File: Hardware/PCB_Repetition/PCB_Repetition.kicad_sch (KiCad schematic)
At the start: 45 parts, among them J1 Conn_01x03, SW1 SW_SPST, SW2 SW_SPST, U3 PCF8575DBR

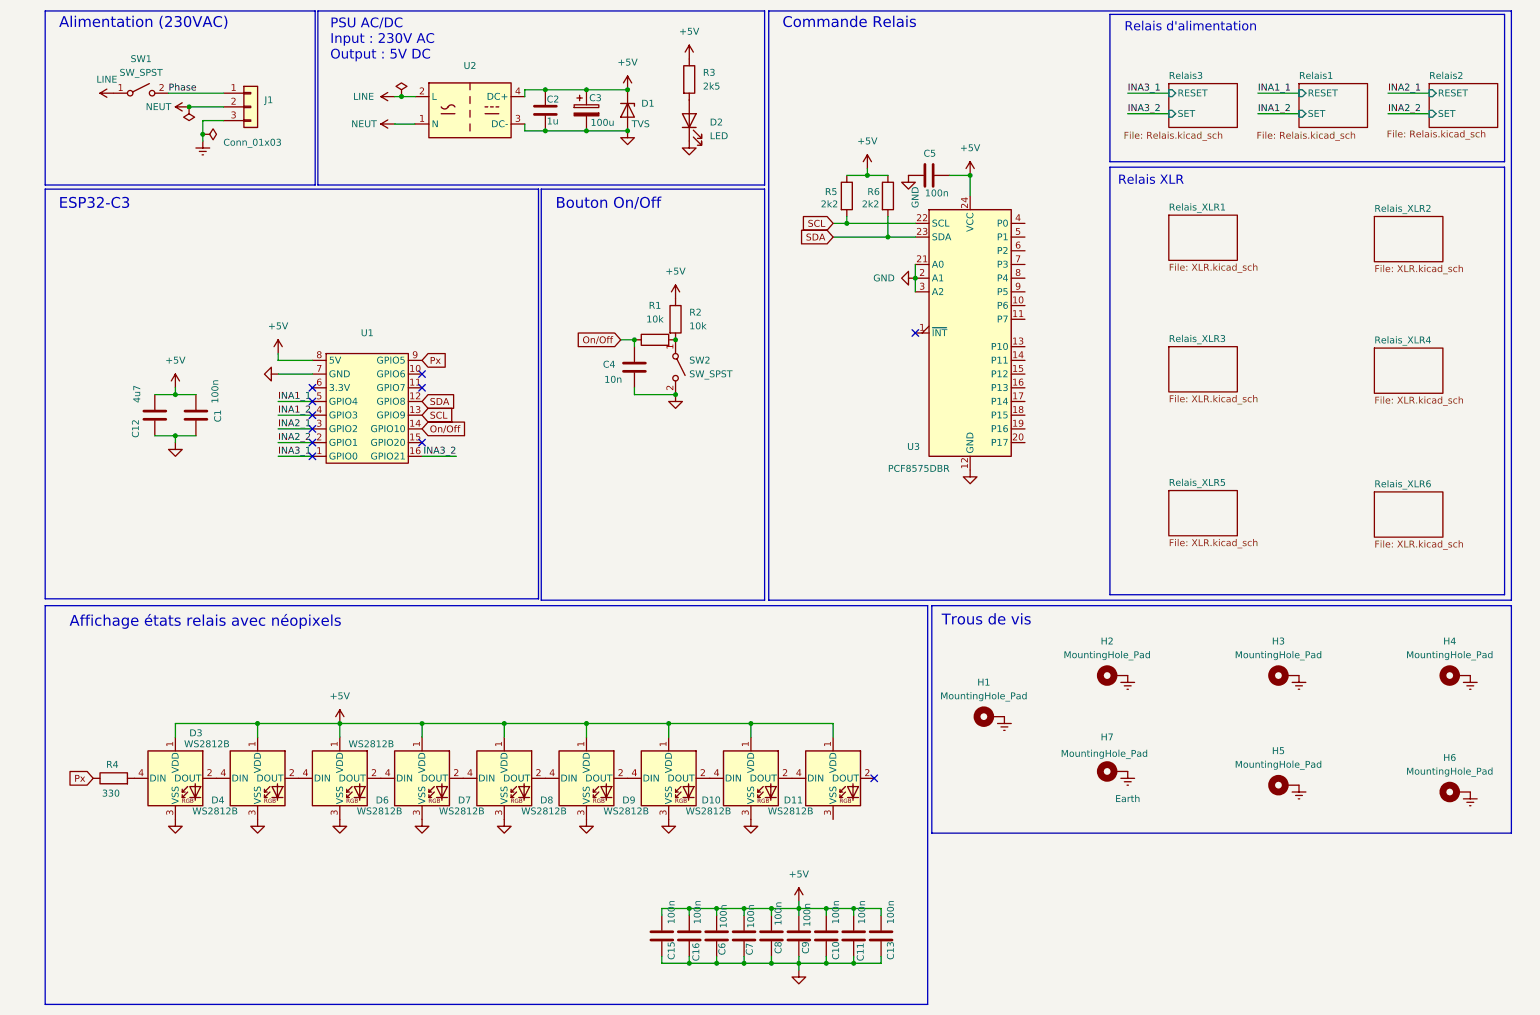
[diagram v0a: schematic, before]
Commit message: ajout des pulldown sur les transistors
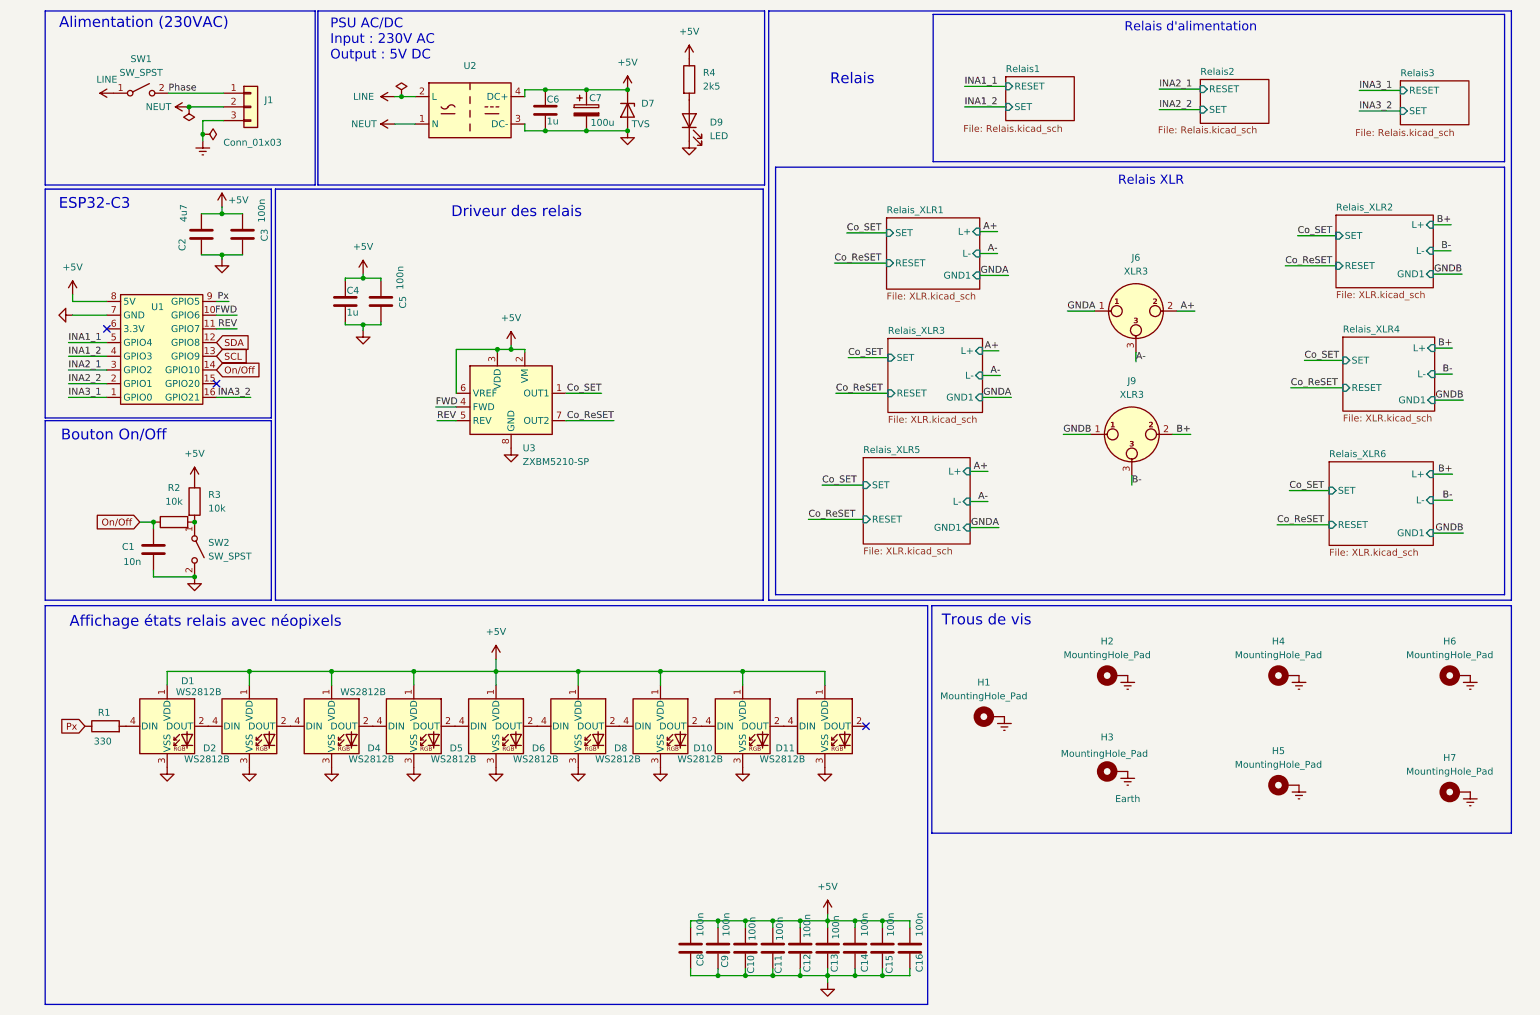
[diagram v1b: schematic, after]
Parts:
- removed R5, R6: 2k2, Resistor_SMD:R_0603_1608Metric_Pad0.98x0.95mm_HandSolder, symbol Device:R
- removed U3: PCF8575DBR, Package_SO:SSOP-24_5.3x8.2mm_P0.65mm, symbol Interface_Expansion:PCF8575DBR
- added C4: 1u, Capacitor_SMD:C_0201_0603Metric_Pad0.64x0.40mm_HandSolder, symbol Device:C
- added J6, J9: XLR3, Connector_Audio:Jack_XLR_Neutrik_NC3FAAV_Vertical, symbol Connector_Audio:XLR3
- added U3: ZXBM5210-SP, Package_SO:Diodes_SO-8EP, symbol Driver_Motor:ZXBM5210-SP
- renumbered C4 to C1, C6 to C10, C7 to C11, C8 to C12, C9 to C13, C10 to C14, C11 to C15, C13 to C16, C12 to C2, C1 to C3, C2 to C6, C3 to C7, C15 to C8, C16 to C9, D3 to D1, D4 to D2, D5 to D3, D6 to D4, D7 to D5, D8 to D6, D1 to D7, D9 to D8, D2 to D9, H7 to H3, H3 to H4, H4 to H6, H6 to H7, R4 to R1, R1 to R2, R2 to R3, R3 to R4
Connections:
- net +5V: now also C5.1, C4.1, U3.2 (VM), U3.3 (VDD), U3.6 (VREF); no longer C5.2
- net GND: now also C5.2, D11.3 (VSS), C4.2, U3.8 (GND), U3.9 (GND); no longer C5.1
- net FWD: now reaches U1.10 (GPIO6)
- net FWD: now also U3.4 (FWD)
- net REV: now reaches U1.11 (GPIO7)
- net REV: now also U3.5 (REV)
- new net A+: J6.2
- new net A-: J6.3
- new net B+: J9.2
- new net B-: J9.3
- new net Co_ReSET: U3.7 (OUT2)
- new net Co_SET: U3.1 (OUT1)
- new net GNDA: J6.1
- new net GNDB: J9.1
- no-connect marks 11 -> 3
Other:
- sheet Relais_XLR1 ports: added GND1, L+, L-, RESET, SET; removed none
- sheet Relais_XLR2 ports: added GND1, L+, L-, RESET, SET; removed none
- sheet Relais_XLR3 ports: added GND1, L+, L-, RESET, SET; removed none
- sheet Relais_XLR4 ports: added GND1, L+, L-, RESET, SET; removed none
- sheet Relais_XLR5 ports: added GND1, L+, L-, RESET, SET; removed none
- sheet Relais_XLR6 ports: added GND1, L+, L-, RESET, SET; removed none
- note added: "Driveur des relais"
- note added: "Relais"
- note removed: "Commande Relais"
- moved on the sheet: C1, C10, C11, C12, C13, C14, C15, C16, C2, C3, C8, C9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

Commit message: finalisation PCB-salle de Répétition
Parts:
- removed U1: ~, ESP32_C3_SuperMini:SuperMini SMT, symbol ESP32_C3_SuperMini:SuperMini_1
- removed U2: ~, AC_DC_module:MP-LDE06-20B05, symbol AC-DC-5V:U_1
- added C17, C18: 100n, Capacitor_SMD:C_0603_1608Metric_Pad1.08x0.95mm_HandSolder, symbol Device:C
- added D12: WS2812B, LED_SMD:LED_WS2812B_PLCC4_5.0x5.0mm_P3.2mm, symbol LED:WS2812B
- added R5, R6: 2k2, Resistor_SMD:R_0603_1608Metric_Pad0.98x0.95mm_HandSolder, symbol Device:R
- added U1: ~, ESP32_SuperMini:SuperMini SMT, symbol ESP32_C3:SuperMini_1
- added U3: ~, AD-DC_Module:MP-LDE06-20B05, symbol Module_AC_DC:U_1
- added U4: PCF8575DBR, Package_SO:SSOP-24_5.3x8.2mm_P0.65mm, symbol Interface_Expansion:PCF8575DBR
- C4, C6: footprint Capacitor_SMD:C_0201_0603Metric_Pad0.64x0.40mm_HandSolder -> Capacitor_SMD:C_0603_1608Metric_Pad1.08x0.95mm_HandSolder
- J1: footprint Conn_Alim:Conn_Secteur -> Conn_secteur:Conn_Secteur
- renumbered J9 to J2, J6 to J3, U3 to U2
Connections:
- net +5V: now also C17.2, C18.1, D12.1 (VDD), R5.1, R6.1, U1.8 (5V), U3.4 (DC+), U4.24 (VCC)
- net Earth: no longer H1.1, H2.1, H4.1, H5.1, H6.1, H7.1
- net FWD: now also U1.10 (GPIO6)
- net GND: now also H1.1, H4.1, H5.1, H6.1, H7.1, C17.1, C18.2, D12.3 (VSS), U1.7 (GND), U3.3 (DC-), U4.12 (GND), U4.2 (A1), U4.21 (A0), U4.3 (A2)
- net INA1_1: now also U4.9 (P5)
- net INA1_2: now also U4.8 (P4)
- net INA2_1: now also U4.7 (P3)
- net INA2_2: now also U4.6 (P2)
- net INA3_1: now also U4.20 (P17)
- net INA3_2: now also U4.19 (P16)
- net LINE: now also U3.2 (L)
- net NEUT: now also U3.1 (N)
- net On/Off: now also U1.14 (GPIO10)
- net Px: now also U1.9 (GPIO5)
- net REV: now also U1.11 (GPIO7)
- net SCL: now also R5.2, U1.13 (GPIO9), U4.22 (SCL)
- net SDA: now also R6.2, U1.12 (GPIO8), U4.23 (SDA)
- net at D11.2 (DOUT): now also D12.4 (DIN)
- no-connect marks 3 -> 21
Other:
- note added: "Commande Relais et Relais XLR"
- note removed: "Relais XLR"
- moved on the sheet: C1, C10, C11, C12, C13, C14, C15, C16, C2, C3, C5, C6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

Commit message: finalisation v2 PCB repetition
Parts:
- removed C13, C14, C15, C16, C18: 100n, Capacitor_SMD:C_0603_1608Metric_Pad1.08x0.95mm_HandSolder, symbol Device:C
- removed D10, D11, D12, D6, D8: WS2812B, LED_SMD:LED_WS2812B_PLCC4_5.0x5.0mm_P3.2mm, symbol LED:WS2812B
- added SW9: SW_DIP_x02, DIP_Switch:DIP_SW_1x02_P2.54mm, symbol Switch:SW_DIP_x02
- U1: footprint ESP32_SuperMini:SuperMini SMT -> ESP32_SuperMini:C3_SuperMini
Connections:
- net Earth: now also H2.1; no longer H3.1
- net FWD: now also U1.11 (GPIO7); no longer U1.10 (GPIO6)
- net GND: now also H3.1, SW9.3, SW9.4
- net GNDA: now also SW9.1
- net GNDB: now also SW9.2
- net INA1_1: now also U4.17 (P14); no longer U4.9 (P5)
- net INA1_2: now also U4.18 (P15); no longer U4.8 (P4)
- net INA2_1: now also U4.19 (P16); no longer U4.7 (P3)
- net INA2_2: now also U4.20 (P17); no longer U4.6 (P2)
- net INA3_1: now also U4.6 (P2); no longer U4.20 (P17)
- net INA3_2: now also U4.7 (P3); no longer U4.19 (P16)
- net REV: now also U1.10 (GPIO6); no longer U1.11 (GPIO7)
- no-connect marks 21 -> 20
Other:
- sheet Relais_XLR1 ports: added none; removed GND1
- sheet Relais_XLR2 ports: added none; removed GND1
- sheet Relais_XLR3 ports: added none; removed GND1
- sheet Relais_XLR4 ports: added none; removed GND1
- sheet Relais_XLR5 ports: added none; removed GND1
- sheet Relais_XLR6 ports: added none; removed GND1
- moved on the sheet: C10, C11, C12, C8, C9, D1, D2, D4, D5, H2, H3, J2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

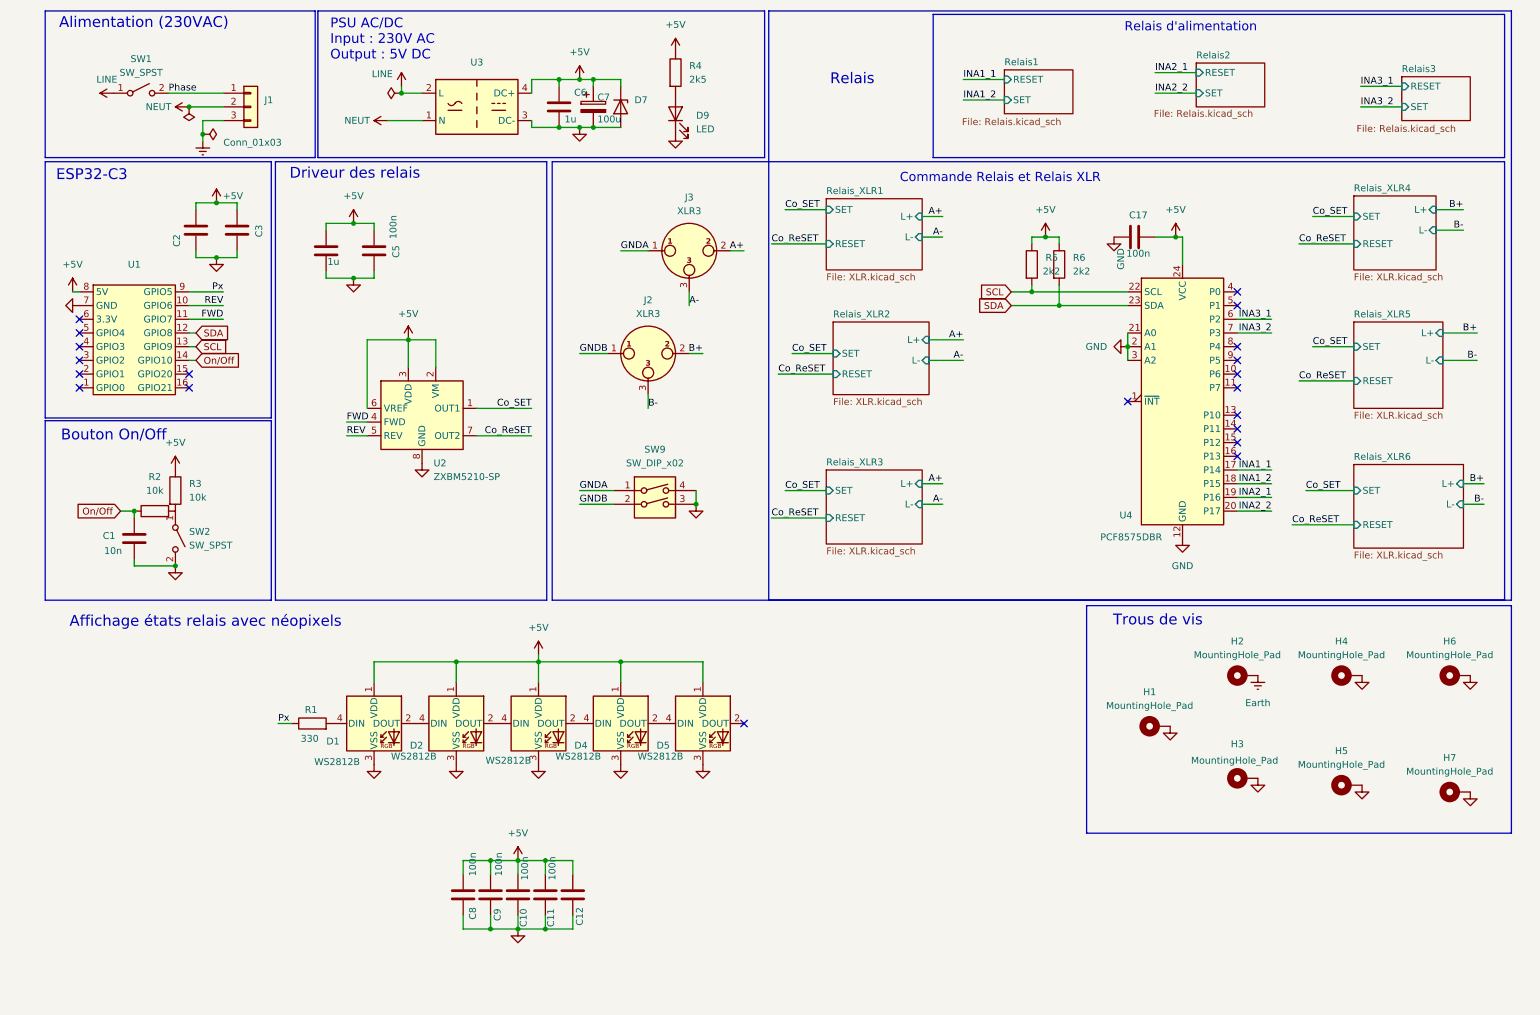
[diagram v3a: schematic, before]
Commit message: ajout des pinheaders en plus
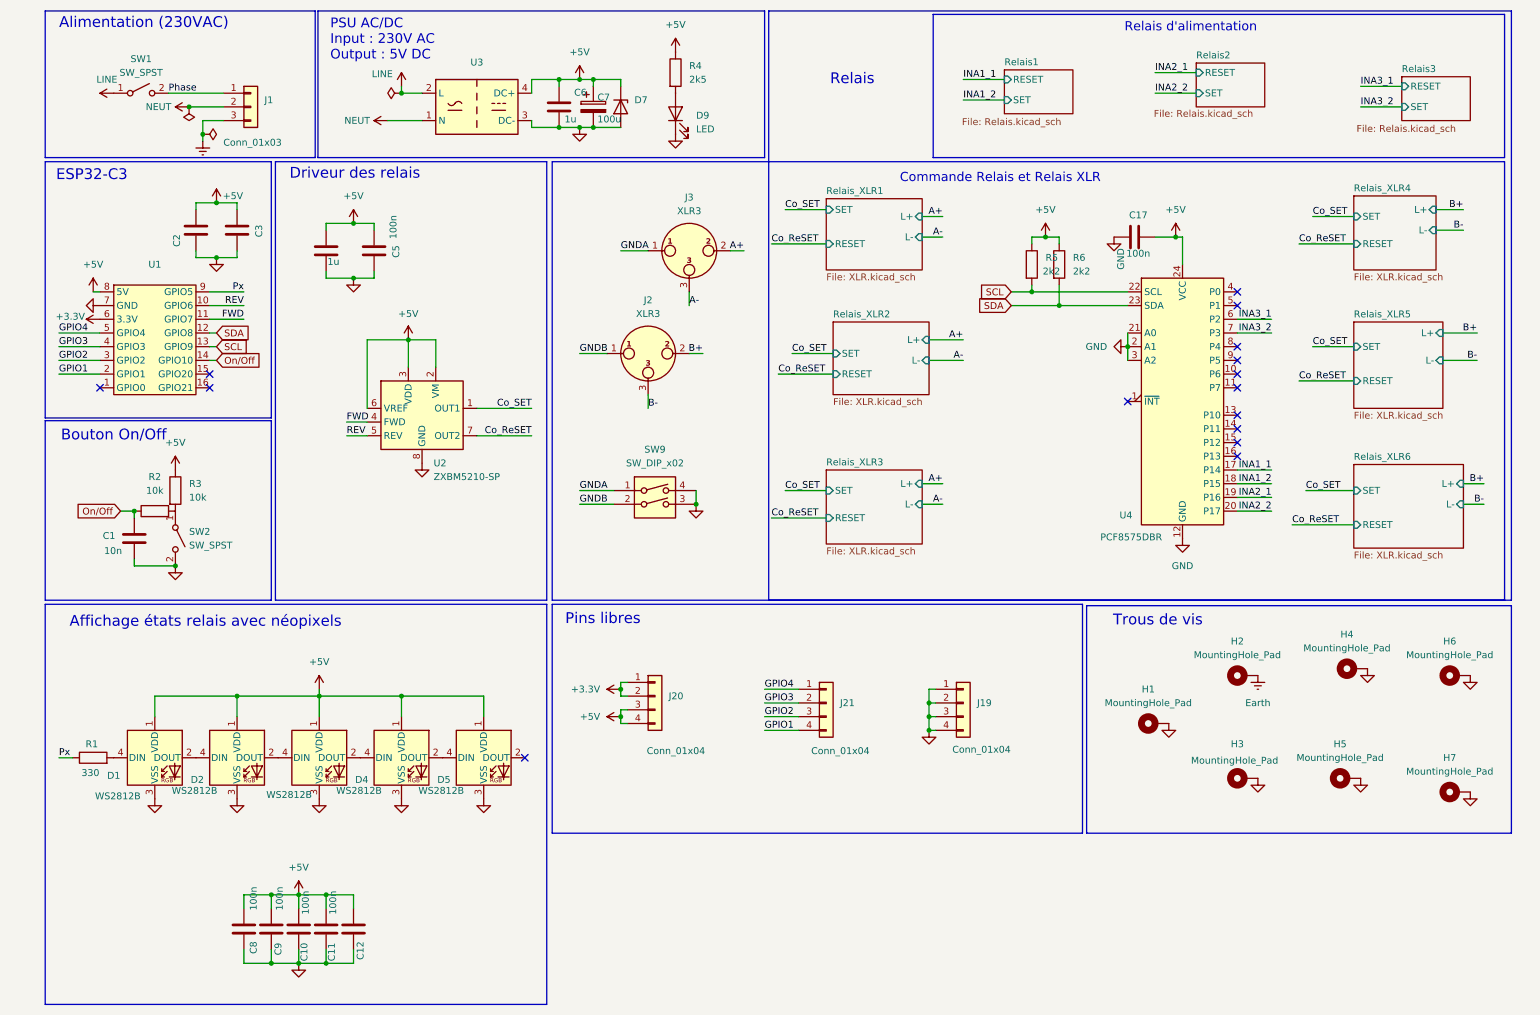
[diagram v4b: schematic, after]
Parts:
- added J19, J20, J21: Conn_01x04, Connector_PinHeader_2.54mm:PinHeader_1x04_P2.54mm_Vertical, symbol Connector_Generic:Conn_01x04
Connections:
- net +5V: now also J20.3 (Pin_3), J20.4 (Pin_4)
- net GND: now also J19.1 (Pin_1), J19.2 (Pin_2), J19.3 (Pin_3), J19.4 (Pin_4)
- net GPIO1: now reaches U1.2 (GPIO1)
- net GPIO1: now also J21.4 (Pin_4)
- net GPIO2: now reaches U1.3 (GPIO2)
- net GPIO2: now also J21.3 (Pin_3)
- net GPIO3: now reaches U1.4 (GPIO3)
- net GPIO3: now also J21.2 (Pin_2)
- net GPIO4: now reaches U1.5 (GPIO4)
- net GPIO4: now also J21.1 (Pin_1)
- net +3.3V: now reaches U1.6 (3.3V)
- net +3.3V: now also J20.1 (Pin_1), J20.2 (Pin_2)
- no-connect marks 20 -> 15
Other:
- note added: "Pins libres"
- moved on the sheet: C10, C11, C12, C8, C9, D1, D2, D4, D5, H1, H4, H5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

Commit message: correction orientation des connecteurs sur secteur
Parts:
- D9: footprint LED_SMD:LED_0603_1608Metric_Pad1.05x0.95mm_HandSolder -> img:LED_0603_avec_dessin
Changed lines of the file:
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@@
 			)
 		)
-		(property "Footprint" "LED_SMD:LED_0603_1608Metric_Pad1.05x0.95mm_HandSolder"
+		(property "Footprint" "img:LED_0603_avec_dessin"
 			(at 129.54 31.75 0)
 			(effects
